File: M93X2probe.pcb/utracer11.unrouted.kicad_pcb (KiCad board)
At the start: 4 copper layers, 132.3 x 214.1 mm, 129 parts, among them J1 PWR, J10 UB_MISC, J11 CONN-DEC-DUAL-AB, J12 UB_BR, J13 UB_BG, J14 UB_DMA, J15 Arduino AUX, J16 Arduino-5V-Power, J18 UART, J19 KY11 M7859.J2, J2 GND, J20 KY11 M7859.J3, J21 CPU M8266.J1, J22 CPU M8266.J2, J23 KM11.A, J24 KM11.B, J25 MUD-BG4, J26 MUD-BG5, J27 MUD-BG6, J28 MUD-BG7, J29 MUD-NPG, J3 GND, J30 BOOT SW., J31 RETURN, J4 UB_DATA, J5 UB_PAB, J6 UB_ADDR, J7 UB_C01, J8 UB_MSYN, J9 UB_SKBYINT, SW1 Reset, SW2 Function, U1 74LS138, U10 MCP23017-1.0, U11 MCP23017-0.1, U12 MCP23017-0.3, U13 74HCT374, U14 74HCT374, U15 MCP23017-1.2, U16 MCP23017-1.1, U17 ULN2803A, U18 ULN2803A, U19 ULN2803A, U2 74HCT30, U20 ULN2803A, U21 ULN2803A, U22 MCP23017-3.0, U23 MCP23017-3.1, U24 MCP23017-3.3, U25 MCP23017-3.2, U26 24LC1025, U3 8837, U4 DEC8881, U5 MAX232, U6 MCP23017-2.0, U7 74LS86, U8 MCP23017-0.0, U9 MCP23017-0.2

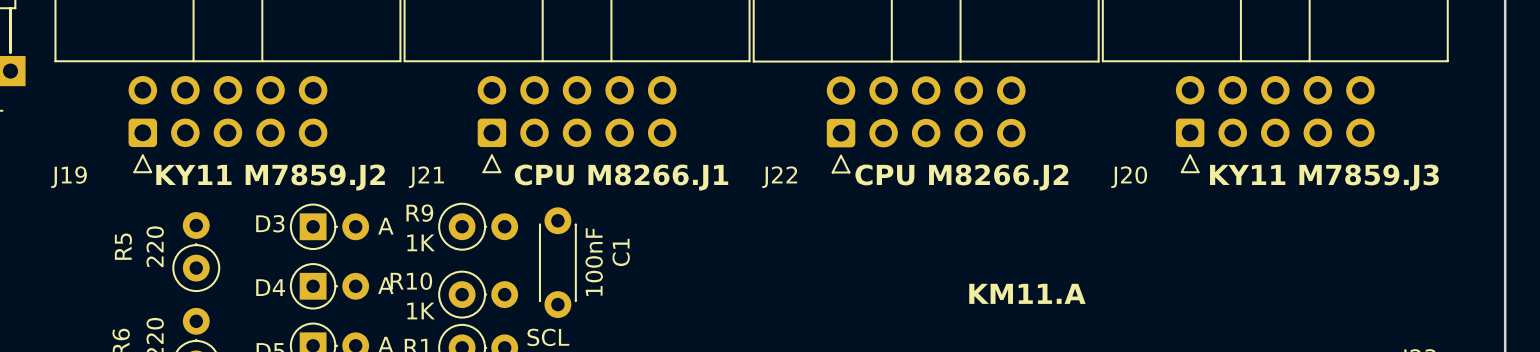
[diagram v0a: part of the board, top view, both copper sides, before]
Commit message: ^repalce synthetic KM11 signals "Inxx, out**" with flipchip pin names
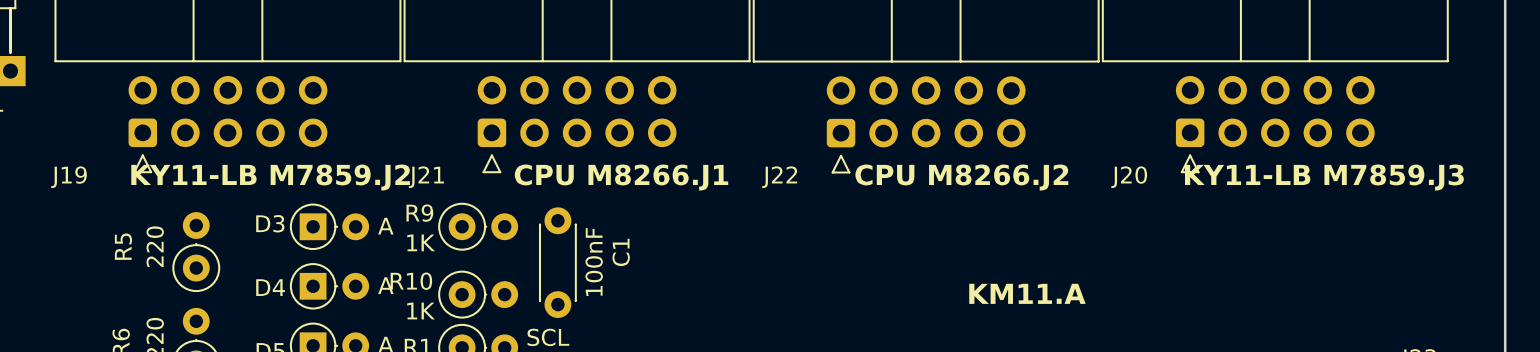
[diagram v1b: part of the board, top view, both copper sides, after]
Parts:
- J19: value KY11 M7859.J2 -> KY11-LB M7859.J2
- J20: value KY11 M7859.J3 -> KY11-LB M7859.J3
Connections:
- net /ucontrol_km11/KM11A_IN00 renamed /ucontrol_km11/KM11A_K2
- net /ucontrol_km11/KM11A_IN01 renamed /ucontrol_km11/KM11A_N1
- net /ucontrol_km11/KM11A_IN02 renamed /ucontrol_km11/KM11A_V1
- net /ucontrol_km11/KM11A_IN03 renamed /ucontrol_km11/KM11A_P2
- net /ucontrol_km11/KM11A_IN10 renamed /ucontrol_km11/KM11A_J1
- net /ucontrol_km11/KM11A_IN11 renamed /ucontrol_km11/KM11A_C1
- net /ucontrol_km11/KM11A_IN12 renamed /ucontrol_km11/KM11A_T2
- net /ucontrol_km11/KM11A_IN13 renamed /ucontrol_km11/KM11A_U2
- net /ucontrol_km11/KM11A_IN20 renamed /ucontrol_km11/KM11A_P1
- net /ucontrol_km11/KM11A_IN21 renamed /ucontrol_km11/KM11A_L1
- net /ucontrol_km11/KM11A_IN22 renamed /ucontrol_km11/KM11A_F1
- net /ucontrol_km11/KM11A_IN23 renamed /ucontrol_km11/KM11A_D1
- net /ucontrol_km11/KM11A_IN30 renamed /ucontrol_km11/KM11A_R1
- net /ucontrol_km11/KM11A_IN31 renamed /ucontrol_km11/KM11A_K1
- net /ucontrol_km11/KM11A_IN32 renamed /ucontrol_km11/KM11A_S2
- net /ucontrol_km11/KM11A_IN33 renamed /ucontrol_km11/KM11A_M1
- net /ucontrol_km11/KM11A_IN40 renamed /ucontrol_km11/KM11A_S1
- net /ucontrol_km11/KM11A_IN41 renamed /ucontrol_km11/KM11A_M2
- net /ucontrol_km11/KM11A_IN42 renamed /ucontrol_km11/KM11A_F2
- net /ucontrol_km11/KM11A_IN43 renamed /ucontrol_km11/KM11A_E1
- net /ucontrol_km11/KM11A_IN50 renamed /ucontrol_km11/KM11A_N2
- net /ucontrol_km11/KM11A_IN51 renamed /ucontrol_km11/KM11A_D2
- net /ucontrol_km11/KM11A_IN52 renamed /ucontrol_km11/KM11A_H2
- net /ucontrol_km11/KM11A_IN53 renamed /ucontrol_km11/KM11A_J2
- net /ucontrol_km11/KM11A_IN60 renamed /ucontrol_km11/KM11A_R2
- net /ucontrol_km11/KM11A_IN61 renamed /ucontrol_km11/KM11A_E2
- net /ucontrol_km11/KM11A_IN62 renamed /ucontrol_km11/KM11A_H1
- net /ucontrol_km11/KM11A_IN63 renamed /ucontrol_km11/KM11A_L2
- net /ucontrol_km11/KM11A_OUT00_L renamed /ucontrol_km11/KM11A_A1_L
- net /ucontrol_km11/KM11A_OUT01_L renamed /ucontrol_km11/KM11A_B2_L
- net /ucontrol_km11/KM11A_OUT10 renamed /ucontrol_km11/KM11A_U1_L
- net /ucontrol_km11/KM11A_OUT11_L renamed /ucontrol_km11/KM11A_V2_L
- net /ucontrol_km11/KM11B_IN00 renamed /ucontrol_km11/KM11B_K2
- net /ucontrol_km11/KM11B_IN01 renamed /ucontrol_km11/KM11B_N1
- net /ucontrol_km11/KM11B_IN02 renamed /ucontrol_km11/KM11B_V1
- net /ucontrol_km11/KM11B_IN03 renamed /ucontrol_km11/KM11B_P2
- net /ucontrol_km11/KM11B_IN10 renamed /ucontrol_km11/KM11B_J1
- net /ucontrol_km11/KM11B_IN11 renamed /ucontrol_km11/KM11B_C1
- net /ucontrol_km11/KM11B_IN12 renamed /ucontrol_km11/KM11B_T2
- net /ucontrol_km11/KM11B_IN13 renamed /ucontrol_km11/KM11B_U2
- net /ucontrol_km11/KM11B_IN20 renamed /ucontrol_km11/KM11B_P1
- net /ucontrol_km11/KM11B_IN21 renamed /ucontrol_km11/KM11B_L1
- net /ucontrol_km11/KM11B_IN22 renamed /ucontrol_km11/KM11B_F1
- net /ucontrol_km11/KM11B_IN23 renamed /ucontrol_km11/KM11B_D1
- net /ucontrol_km11/KM11B_IN30 renamed /ucontrol_km11/KM11B_R1
- net /ucontrol_km11/KM11B_IN31 renamed /ucontrol_km11/KM11B_K1
- net /ucontrol_km11/KM11B_IN32 renamed /ucontrol_km11/KM11B_S2
- net /ucontrol_km11/KM11B_IN33 renamed /ucontrol_km11/KM11B_M1
- net /ucontrol_km11/KM11B_IN40 renamed /ucontrol_km11/KM11B_S1
- net /ucontrol_km11/KM11B_IN41 renamed /ucontrol_km11/KM11B_M2
- net /ucontrol_km11/KM11B_IN42 renamed /ucontrol_km11/KM11B_F2
- net /ucontrol_km11/KM11B_IN43 renamed /ucontrol_km11/KM11B_E1
- net /ucontrol_km11/KM11B_IN50 renamed /ucontrol_km11/KM11B_N2
- net /ucontrol_km11/KM11B_IN51 renamed /ucontrol_km11/KM11B_D2
- net /ucontrol_km11/KM11B_IN52 renamed /ucontrol_km11/KM11B_H2
- net /ucontrol_km11/KM11B_IN53 renamed /ucontrol_km11/KM11B_J2
- net /ucontrol_km11/KM11B_IN60 renamed /ucontrol_km11/KM11B_R2
- net /ucontrol_km11/KM11B_IN61 renamed /ucontrol_km11/KM11B_E2
- net /ucontrol_km11/KM11B_IN62 renamed /ucontrol_km11/KM11B_H1
- net /ucontrol_km11/KM11B_IN63 renamed /ucontrol_km11/KM11B_L2
- net /ucontrol_km11/KM11B_OUT00_L renamed /ucontrol_km11/KM11B_A1_L
- net /ucontrol_km11/KM11B_OUT01_L renamed /ucontrol_km11/KM11B_B2_L
- net /ucontrol_km11/KM11B_OUT10 renamed /ucontrol_km11/KM11B_U1_L
- net /ucontrol_km11/KM11B_OUT11_L renamed /ucontrol_km11/KM11B_V2_L
